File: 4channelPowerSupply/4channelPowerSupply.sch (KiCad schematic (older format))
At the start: 0 parts

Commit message: Added main components
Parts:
- added C? (x4): 4.7uF, Capacitor_SMD:C_0603_1608Metric, symbol Device:C
- added C?: 10uF, Capacitor_SMD:C_0603_1608Metric, symbol Device:C
- added C?: 2200pF, Capacitor_SMD:C_0603_1608Metric, symbol Device:C
- added C? (x2): 22pF, Capacitor_SMD:C_0603_1608Metric, symbol Device:C
- added C?: 47uF, Capacitor_SMD:C_0603_1608Metric, symbol Device:C
- added C?: 10pF, Capacitor_SMD:C_0603_1608Metric, symbol Device:C
- added C? (x3): 22uF, Capacitor_SMD:C_0603_1608Metric, symbol Device:C
- added C? (x2): 0.1uF, Capacitor_SMD:C_0603_1608Metric, symbol Device:C
- added C?: 4.7pF, Capacitor_SMD:C_0603_1608Metric, symbol Device:C
- added L?: PM1008S-1R8M-RC, Inductor_SMD:L_1008_2520Metric_Pad1.43x2.20mm_HandSolder, symbol Device:L
- added L? (x2): LPS4018-222MRC, Inductor_SMD:L_Coilcraft_XxL4020, symbol Device:L
- added L?: SDR7030-6R2M, Inductor_SMD:L_Bourns_SRP7028A_7.3x6.6mm, symbol Device:L
- added R?: 60.4, Resistor_SMD:R_0603_1608Metric, symbol Device:R
- added R?: 20K, Resistor_SMD:R_0603_1608Metric, symbol Device:R
- added R? (x2): 100K, Resistor_SMD:R_0603_1608Metric, symbol Device:R
- added R?: 249K, Resistor_SMD:R_0603_1608Metric, symbol Device:R
- added R?: 200K, Resistor_SMD:R_0603_1608Metric, symbol Device:R
- added R?: 316K, Resistor_SMD:R_0603_1608Metric, symbol Device:R
- added R?: 137K, Resistor_SMD:R_0603_1608Metric, symbol Device:R
- added R?: 453K, Resistor_SMD:R_0603_1608Metric, symbol Device:R
- added R?: 113K, Resistor_SMD:R_0603_1608Metric, symbol Device:R
- added U?: LT8602EUJ#PBF, Package_DFN_QFN:QFN-40-1EP_6x6mm_P0.5mm_EP4.6x4.6mm_ThermalVias, symbol locallib:LT8602EUJ#PBF
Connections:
- net labels added: GND
- wire segments 0 -> 136
- no-connect marks 0 -> 5

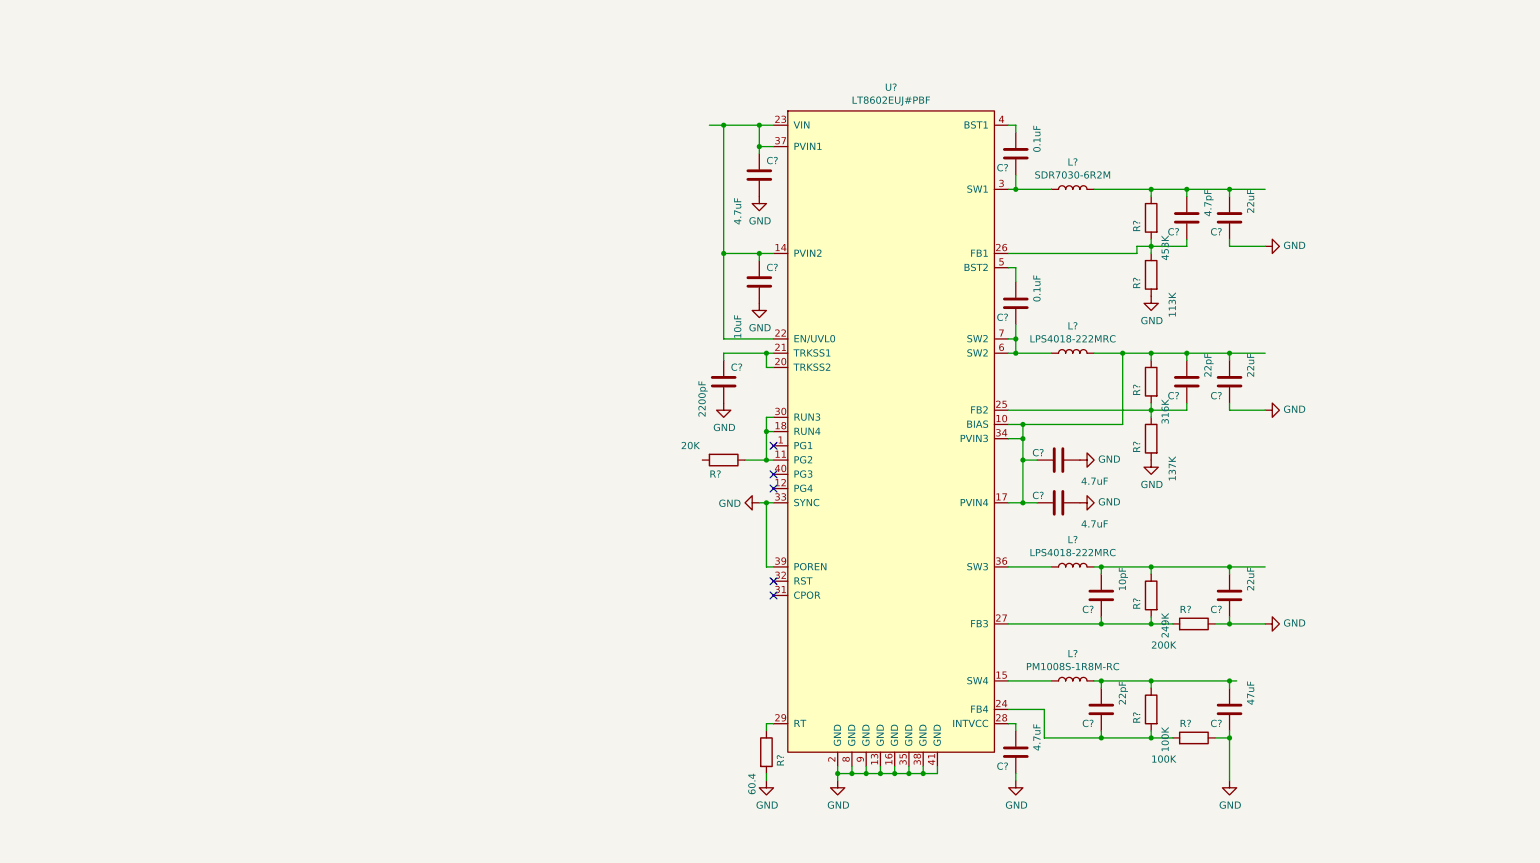
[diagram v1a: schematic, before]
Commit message: Net generated and added all components
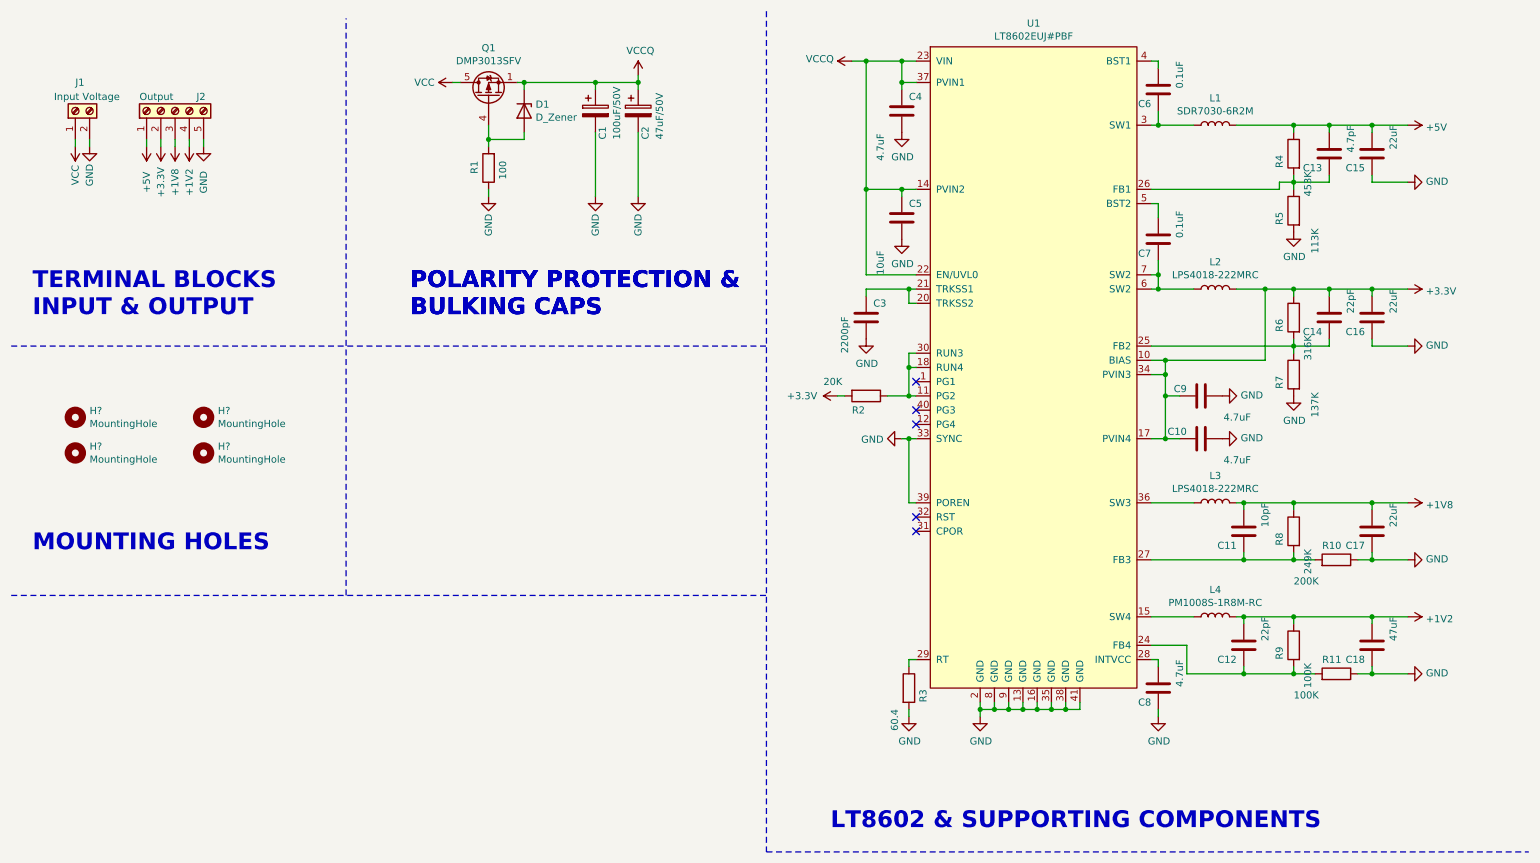
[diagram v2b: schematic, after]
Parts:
- added C1: 100uF/50V, Capacitor_SMD:C_Elec_6.3x5.4, symbol Device:CP
- added C2: 47uF/50V, Capacitor_SMD:C_Elec_6.3x5.4, symbol Device:CP
- added D1: D_Zener, symbol Device:D_Zener
- added H? (x4): MountingHole, MountingHole:MountingHole_3.2mm_M3_Pad_Via, symbol Mechanical:MountingHole
- added J1: Input Voltage, TerminalBlock_Phoenix:TerminalBlock_Phoenix_MKDS-1,5-2_1x02_P5.00mm_Horizontal, symbol Connector:Screw_Terminal_01x02
- added J2: Output, TerminalBlock_Phoenix:TerminalBlock_Phoenix_MKDS-1,5-5-5.08_1x05_P5.08mm_Horizontal, symbol Connector:Screw_Terminal_01x05
- added Q1: DMP3013SFV, Package_SON:Diodes_PowerDI3333-8, symbol Transistor_FET:DMP3013SFV
- added R1: 100, Resistor_SMD:R_0603_1608Metric, symbol Device:R
- gave numbers to parts that had none: 31
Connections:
- net labels added: +1V2, +1V8, +3.3V, +5V, VCC, VCCQ
- wire segments 136 -> 159
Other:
- note added: "LT8602 & SUPPORTING COMPONENTS"
- note added: "MOUNTING HOLES"
- note added: "POLARITY PROTECTION &\nBULKING CAPS\n"
- note added: "TERMINAL BLOCKS\nINPUT & OUTPUT"
- moved on the sheet: C10, C11, C12, C13, C14, C15, C16, C17, C18, C3, C4, C5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

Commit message: Added indication
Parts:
- added D? (x4): LED, LED_SMD:LED_0603_1608Metric, symbol Device:LED
- added R?: 900, Resistor_SMD:R_0603_1608Metric, symbol Device:R
- added R?: 600, Resistor_SMD:R_0603_1608Metric, symbol Device:R
- added R?: 1K5, Resistor_SMD:R_0603_1608Metric, symbol Device:R
- added R?: 2K5, Resistor_SMD:R_0603_1608Metric, symbol Device:R
- gave numbers to parts that had none: 4
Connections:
- net +1V2: now also R?.1
- net +1V8: now also R?.1
- net +3V3: now also R?.1
- net +5V: now also R?.1
- net GND: now also D?.1 (K), D?.1 (K), D?.1 (K), D?.1 (K)
- new net: D?.2 (A), R?.2 (x4)
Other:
- note added: "POWER INDICATION\n"
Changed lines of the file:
@@
 	1    0    0    -1
 $EndComp
-Text Notes 650  2650 0    118  ~ 24
+Text Notes 550  2750 0    118  ~ 24
 TERMINAL BLOCKS\nINPUT & OUTPUT
-Text Notes 3300 2650 0    118  ~ 24
-POLARITY PROTECTION &\nBULKING CAPS\n
-Text Notes 3300 2650 0    118  ~ 24
+Text Notes 2950 2750 0    118  ~ 24
 POLARITY PROTECTION &\nBULKING CAPS\n
 Text Notes 6250 6250 0    118  ~ 24
 LT8602 & SUPPORTING COMPONENTS
 $Comp
-L Mechanical:MountingHole H?
+L Mechanical:MountingHole H1
 U 1 1 60D5E110
 P 950 3350
-F 0 "H?" H 1050 3396 50  0000 L CNN
+F 0 "H1" H 1050 3396 50  0000 L CNN
 F 1 "MountingHole" H 1050 3305 50  0000 L CNN
 F 2 "MountingHole:MountingHole_3.2mm_M3_Pad_Via" H 950 3350 50  0001 C CNN
@@
 $EndComp
 $Comp
-L Mechanical:MountingHole H?
+L Mechanical:MountingHole H3
 U 1 1 60D5E583
 P 1850 3350
-F 0 "H?" H 1950 3396 50  0000 L CNN
+F 0 "H3" H 1950 3396 50  0000 L CNN
 F 1 "MountingHole" H 1950 3305 50  0000 L CNN
 F 2 "MountingHole:MountingHole_3.2mm_M3_Pad_Via" H 1850 3350 50  0001 C CNN
@@
 $EndComp
 $Comp
-L Mechanical:MountingHole H?
+L Mechanical:MountingHole H2
 U 1 1 60D5E8C4
 P 950 3600
-F 0 "H?" H 1050 3646 50  0000 L CNN
+F 0 "H2" H 1050 3646 50  0000 L CNN
 F 1 "MountingHole" H 1050 3555 50  0000 L CNN
 F 2 "MountingHole:MountingHole_3.2mm_M3_Pad_Via" H 950 3600 50  0001 C CNN
@@
 $EndComp
 $Comp
-L Mechanical:MountingHole H?
+L Mechanical:MountingHole H4
 U 1 1 60D5EBB4
 P 1850 3600
-F 0 "H?" H 1950 3646 50  0000 L CNN
+F 0 "H4" H 1950 3646 50  0000 L CNN
 F 1 "MountingHole" H 1950 3555 50  0000 L CNN
 F 2 "MountingHole:MountingHole_3.2mm_M3_Pad_Via" H 1850 3600 50  0001 C CNN
@@
 	1    0    0    -1
 $EndComp
-Text Notes 650  4300 0    118  ~ 24
+Text Notes 550  4500 0    118  ~ 24
 MOUNTING HOLES
 Wire Notes Line
@@
 Wire Notes Line
 	2850 4600 2850 550
+$Comp
+L power:+5V #PWR?
+U 1 1 60D89EAC
+P 4650 3300
+F 0 "#PWR?" H 4650 3150 50  0001 C CNN
+F 1 "+5V" V 4650 3550 50  0000 C CNN
+F 2 "" H 4650 3300 50  0001 C CNN
+F 3 "" H 4650 3300 50  0001 C CNN
+	1    4650 3300
+	1    0    0    -1
+$EndComp
+$Comp
+L power:+3.3V #PWR?
+U 1 1 60D89EB6
+P 4350 3300
+F 0 "#PWR?" H 4350 3150 50  0001 C CNN
+F 1 "+3.3V" V 4350 3550 50  0000 C CNN
+F 2 "" H 4350 3300 50  0001 C CNN
+F 3 "" H 4350 3300 50  0001 C CNN
+	1    4350 3300
+	1    0    0    -1
+$EndComp
+$Comp
+L power:+1V8 #PWR?
+U 1 1 60D89EC0
+P 4050 3300
+F 0 "#PWR?" H 4050 3150 50  0001 C CNN
+F 1 "+1V8" V 4050 3550 50  0000 C CNN
+F 2 "" H 4050 3300 50  0001 C CNN
+F 3 "" H 4050 3300 50  0001 C CNN
+	1    4050 3300
+	1    0    0    -1
+$EndComp
+$Comp
+L power:+1V2 #PWR?
+U 1 1 60D89ECA
+P 3750 3300
+F 0 "#PWR?" H 3750 3150 50  0001 C CNN
+F 1 "+1V2" V 3750 3550 50  0000 C CNN
+F 2 "" H 3750 3300 50  0001 C CNN
+F 3 "" H 3750 3300 50  0001 C CNN
+	1    3750 3300
+	1    0    0    -1
+$EndComp
+$Comp
+L Device:R R?
+U 1 1 60D92CCC
+P 4050 3500
+F 0 "R?" H 4120 3546 50  0000 L CNN
+F 1 "900" H 4120 3455 50  0000 L CNN
+F 2 "Resistor_SMD:R_0603_1608Metric" V 3980 3500 50  0001 C CNN
+F 3 "~" H 4050 3500 50  0001 C CNN
+F 4 "900OHM/1/4W" H 4050 3500 50  0001 C CNN "Characteristics"
+	1    4050 3500
+	1    0    0    -1
+$EndComp
+$Comp
+L Device:R R?
+U 1 1 60D9351C
+P 3750 3500
+F 0 "R?" H 3820 3546 50  0000 L CNN
+F 1 "600" H 3820 3455 50  0000 L CNN
+F 2 "Resistor_SMD:R_0603_1608Metric" V 3680 3500 50  0001 C CNN
+F 3 "~" H 3750 3500 50  0001 C CNN
+F 4 "600OHM/1/4W" H 3750 3500 50  0001 C CNN "Characteristics"
+	1    3750 3500
+	1    0    0    -1
+$EndComp
+$Comp
+L Device:R R?
+U 1 1 60D93985
+P 4350 3500
+F 0 "R?" H 4420 3546 50  0000 L CNN
+F 1 "1K5" H 4420 3455 50  0000 L CNN
+F 2 "Resistor_SMD:R_0603_1608Metric" V 4280 3500 50  0001 C CNN
+F 3 "~" H 4350 3500 50  0001 C CNN
+F 4 "1.5KOHM/1/4W" H 4350 3500 50  0001 C CNN "Characteristics"
+	1    4350 3500
+	1    0    0    -1
+$EndComp
+$Comp
+L Device:R R?
+U 1 1 60D93C3B
+P 4650 3500
+F 0 "R?" H 4720 3546 50  0000 L CNN
+F 1 "2K5" H 4720 3455 50  0000 L CNN
+F 2 "Resistor_SMD:R_0603_1608Metric" V 4580 3500 50  0001 C CNN
+F 3 "~" H 4650 3500 50  0001 C CNN
+F 4 "2.5KOHM/1/4W" H 4650 3500 50  0001 C CNN "Characteristics"
+	1    4650 3500
+	1    0    0    -1
+$EndComp
+$Comp
+L Device:LED D?
+U 1 1 60D94C55
+P 3750 3850
+F 0 "D?" V 3800 3800 50  0000 R CNN
+F 1 "LED" V 3700 3800 50  0000 R CNN
+F 2 "LED_SMD:LED_0603_1608Metric" H 3750 3850 50  0001 C CNN
+F 3 "~" H 3750 3850 50  0001 C CNN
+	1    3750 3850
+	0    -1   -1   0
+$EndComp
+$Comp
+L Device:LED D?
+U 1 1 60D952CA
+P 4050 3850
+F 0 "D?" V 4100 3800 50  0000 R CNN
+F 1 "LED" V 4000 3800 50  0000 R CNN
+F 2 "LED_SMD:LED_0603_1608Metric" H 4050 3850 50  0001 C CNN
+F 3 "~" H 4050 3850 50  0001 C CNN
+	1    4050 3850
+	0    -1   -1   0
+$EndComp
+$Comp
+L Device:LED D?
+U 1 1 60D955BC
+P 4350 3850
+F 0 "D?" V 4400 3800 50  0000 R CNN
+F 1 "LED" V 4300 3800 50  0000 R CNN
+F 2 "LED_SMD:LED_0603_1608Metric" H 4350 3850 50  0001 C CNN
+F 3 "~" H 4350 3850 50  0001 C CNN
+	1    4350 3850
+	0    -1   -1   0
+$EndComp
+$Comp
+L Device:LED D?
+U 1 1 60D9581C
+P 4650 3850
+F 0 "D?" V 4700 3800 50  0000 R CNN
+F 1 "LED" V 4600 3800 50  0000 R CNN
+F 2 "LED_SMD:LED_0603_1608Metric" H 4650 3850 50  0001 C CNN
+F 3 "~" H 4650 3850 50  0001 C CNN
+	1    4650 3850
+	0    -1   -1   0
+$EndComp
+$Comp
+L power:GND #PWR?
+U 1 1 60DA5E06
+P 3750 4050
+F 0 "#PWR?" H 3750 3800 50  0001 C CNN
+F 1 "GND" H 3755 3877 50  0000 C CNN
+F 2 "" H 3750 4050 50  0001 C CNN
+F 3 "" H 3750 4050 50  0001 C CNN
+	1    3750 4050
+	1    0    0    -1
+$EndComp
+$Comp
+L power:GND #PWR?
+U 1 1 60DA60E5
+P 4050 4050
+F 0 "#PWR?" H 4050 3800 50  0001 C CNN
+F 1 "GND" H 4055 3877 50  0000 C CNN
+F 2 "" H 4050 4050 50  0001 C CNN
+F 3 "" H 4050 4050 50  0001 C CNN
+	1    4050 4050
+	1    0    0    -1
+$EndComp
+$Comp
+L power:GND #PWR?
+U 1 1 60DA6209
+P 4350 4050
+F 0 "#PWR?" H 4350 3800 50  0001 C CNN
+F 1 "GND" H 4355 3877 50  0000 C CNN
+F 2 "" H 4350 4050 50  0001 C CNN
+F 3 "" H 4350 4050 50  0001 C CNN
+	1    4350 4050
+	1    0    0    -1
+$EndComp
+$Comp
+L power:GND #PWR?
+U 1 1 60DA642B
+P 4650 4050
+F 0 "#PWR?" H 4650 3800 50  0001 C CNN
+F 1 "GND" H 4655 3877 50  0000 C CNN
+F 2 "" H 4650 4050 50  0001 C CNN
+F 3 "" H 4650 4050 50  0001 C CNN
+	1    4650 4050
+	1    0    0    -1
+$EndComp
+Wire Wire Line
+	3750 3300 3750 3350
+Wire Wire Line
+	3750 3650 3750 3700
+Wire Wire Line
+	3750 4000 3750 4050
+Wire Wire Line
+	4050 4050 4050 4000
+Wire Wire Line
+	4050 3700 4050 3650
+Wire Wire Line
+	4050 3350 4050 3300
+Wire Wire Line
+	4350 3300 4350 3350
+Wire Wire Line
+	4350 3650 4350 3700
+Wire Wire Line
+	4350 4000 4350 4050
+Wire Wire Line
+	4650 3350 4650 3300
+Wire Wire Line
+	4650 3650 4650 3700
+Wire Wire Line
+	4650 4000 4650 4050
+Text Notes 2900 4500 0    118  ~ 24
+POWER INDICATION\n
 $EndSCHEMATC

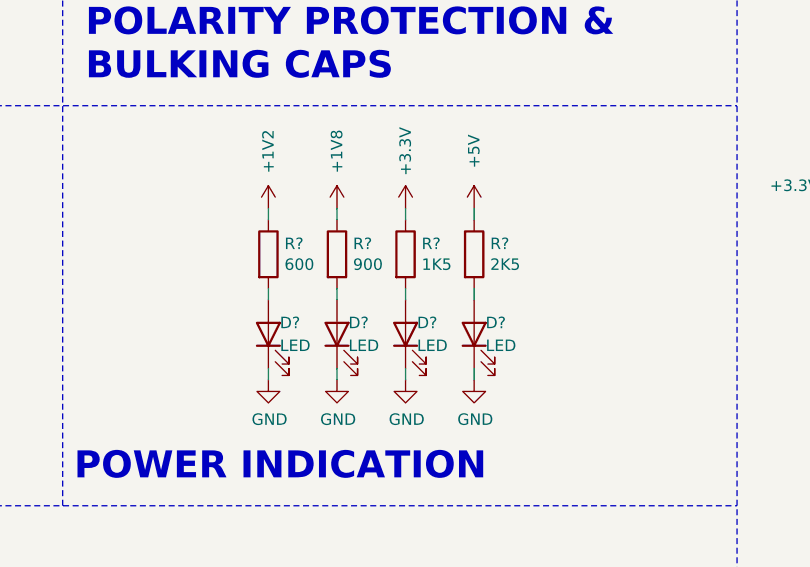
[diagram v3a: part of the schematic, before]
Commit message: Footprint for zener
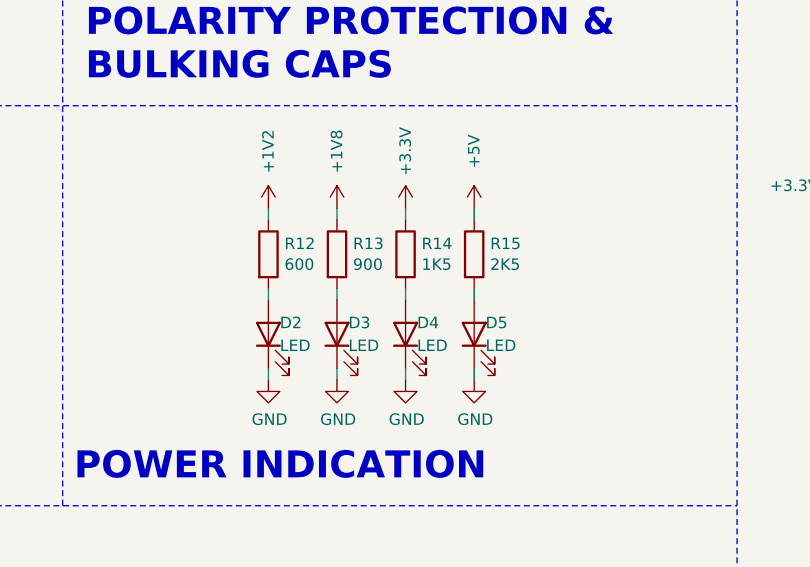
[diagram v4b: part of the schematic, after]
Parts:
- D1: footprint (none) -> Diode_SMD:D_0603_1608Metric
- gave numbers to parts that had none: 8
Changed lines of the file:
@@
 F 0 "D1" V 4054 1280 50  0000 L CNN
 F 1 "D_Zener" V 4145 1280 50  0000 L CNN
-F 2 "" H 4100 1200 50  0001 C CNN
+F 2 "Diode_SMD:D_0603_1608Metric" H 4100 1200 50  0001 C CNN
 F 3 "~" H 4100 1200 50  0001 C CNN
 	1    4100 1200
@@
 	2850 4600 2850 550
 $Comp
-L power:+5V #PWR?
+L power:+5V #PWR0134
 U 1 1 60D89EAC
 P 4650 3300
-F 0 "#PWR?" H 4650 3150 50  0001 C CNN
+F 0 "#PWR0134" H 4650 3150 50  0001 C CNN
 F 1 "+5V" V 4650 3550 50  0000 C CNN
 F 2 "" H 4650 3300 50  0001 C CNN
@@
 $EndComp
 $Comp
-L power:+3.3V #PWR?
+L power:+3.3V #PWR0135
 U 1 1 60D89EB6
 P 4350 3300
-F 0 "#PWR?" H 4350 3150 50  0001 C CNN
+F 0 "#PWR0135" H 4350 3150 50  0001 C CNN
 F 1 "+3.3V" V 4350 3550 50  0000 C CNN
 F 2 "" H 4350 3300 50  0001 C CNN
@@
 $EndComp
 $Comp
-L power:+1V8 #PWR?
+L power:+1V8 #PWR0136
 U 1 1 60D89EC0
 P 4050 3300
-F 0 "#PWR?" H 4050 3150 50  0001 C CNN
+F 0 "#PWR0136" H 4050 3150 50  0001 C CNN
 F 1 "+1V8" V 4050 3550 50  0000 C CNN
 F 2 "" H 4050 3300 50  0001 C CNN
@@
 $EndComp
 $Comp
-L power:+1V2 #PWR?
+L power:+1V2 #PWR0137
 U 1 1 60D89ECA
 P 3750 3300
-F 0 "#PWR?" H 3750 3150 50  0001 C CNN
+F 0 "#PWR0137" H 3750 3150 50  0001 C CNN
 F 1 "+1V2" V 3750 3550 50  0000 C CNN
 F 2 "" H 3750 3300 50  0001 C CNN
@@
 $EndComp
 $Comp
-L Device:R R?
+L Device:R R13
 U 1 1 60D92CCC
 P 4050 3500
-F 0 "R?" H 4120 3546 50  0000 L CNN
+F 0 "R13" H 4120 3546 50  0000 L CNN
 F 1 "900" H 4120 3455 50  0000 L CNN
 F 2 "Resistor_SMD:R_0603_1608Metric" V 3980 3500 50  0001 C CNN
@@
 $EndComp
 $Comp
-L Device:R R?
+L Device:R R12
 U 1 1 60D9351C
 P 3750 3500
-F 0 "R?" H 3820 3546 50  0000 L CNN
+F 0 "R12" H 3820 3546 50  0000 L CNN
 F 1 "600" H 3820 3455 50  0000 L CNN
 F 2 "Resistor_SMD:R_0603_1608Metric" V 3680 3500 50  0001 C CNN
@@
 $EndComp
 $Comp
-L Device:R R?
+L Device:R R14
 U 1 1 60D93985
 P 4350 3500
-F 0 "R?" H 4420 3546 50  0000 L CNN
+F 0 "R14" H 4420 3546 50  0000 L CNN
 F 1 "1K5" H 4420 3455 50  0000 L CNN
 F 2 "Resistor_SMD:R_0603_1608Metric" V 4280 3500 50  0001 C CNN
@@
 $EndComp
 $Comp
-L Device:R R?
+L Device:R R15
 U 1 1 60D93C3B
 P 4650 3500
-F 0 "R?" H 4720 3546 50  0000 L CNN
+F 0 "R15" H 4720 3546 50  0000 L CNN
 F 1 "2K5" H 4720 3455 50  0000 L CNN
 F 2 "Resistor_SMD:R_0603_1608Metric" V 4580 3500 50  0001 C CNN
@@
 $EndComp
 $Comp
-L Device:LED D?
+L Device:LED D2
 U 1 1 60D94C55
 P 3750 3850
-F 0 "D?" V 3800 3800 50  0000 R CNN
+F 0 "D2" V 3800 3800 50  0000 R CNN
 F 1 "LED" V 3700 3800 50  0000 R CNN
 F 2 "LED_SMD:LED_0603_1608Metric" H 3750 3850 50  0001 C CNN
@@
 $EndComp
 $Comp
-L Device:LED D?
+L Device:LED D3
 U 1 1 60D952CA
 P 4050 3850
-F 0 "D?" V 4100 3800 50  0000 R CNN
+F 0 "D3" V 4100 3800 50  0000 R CNN
 F 1 "LED" V 4000 3800 50  0000 R CNN
 F 2 "LED_SMD:LED_0603_1608Metric" H 4050 3850 50  0001 C CNN
@@
 $EndComp
 $Comp
-L Device:LED D?
+L Device:LED D4
 U 1 1 60D955BC
 P 4350 3850
-F 0 "D?" V 4400 3800 50  0000 R CNN
+F 0 "D4" V 4400 3800 50  0000 R CNN
 F 1 "LED" V 4300 3800 50  0000 R CNN
 F 2 "LED_SMD:LED_0603_1608Metric" H 4350 3850 50  0001 C CNN
@@
 $EndComp
 $Comp
-L Device:LED D?
+L Device:LED D5
 U 1 1 60D9581C
 P 4650 3850
-F 0 "D?" V 4700 3800 50  0000 R CNN
+F 0 "D5" V 4700 3800 50  0000 R CNN
 F 1 "LED" V 4600 3800 50  0000 R CNN
 F 2 "LED_SMD:LED_0603_1608Metric" H 4650 3850 50  0001 C CNN
@@
 $EndComp
 $Comp
-L power:GND #PWR?
+L power:GND #PWR0138
 U 1 1 60DA5E06
 P 3750 4050
-F 0 "#PWR?" H 3750 3800 50  0001 C CNN
+F 0 "#PWR0138" H 3750 3800 50  0001 C CNN
 F 1 "GND" H 3755 3877 50  0000 C CNN
 F 2 "" H 3750 4050 50  0001 C CNN
@@
 $EndComp
 $Comp
-L power:GND #PWR?
+L power:GND #PWR0139
 U 1 1 60DA60E5
 P 4050 4050
-F 0 "#PWR?" H 4050 3800 50  0001 C CNN
+F 0 "#PWR0139" H 4050 3800 50  0001 C CNN
 F 1 "GND" H 4055 3877 50  0000 C CNN
 F 2 "" H 4050 4050 50  0001 C CNN
@@
 $EndComp
 $Comp
-L power:GND #PWR?
+L power:GND #PWR0140
 U 1 1 60DA6209
 P 4350 4050
-F 0 "#PWR?" H 4350 3800 50  0001 C CNN
+F 0 "#PWR0140" H 4350 3800 50  0001 C CNN
 F 1 "GND" H 4355 3877 50  0000 C CNN
 F 2 "" H 4350 4050 50  0001 C CNN
@@
 $EndComp
 $Comp
-L power:GND #PWR?
+L power:GND #PWR0141
 U 1 1 60DA642B
 P 4650 4050
-F 0 "#PWR?" H 4650 3800 50  0001 C CNN
+F 0 "#PWR0141" H 4650 3800 50  0001 C CNN
 F 1 "GND" H 4655 3877 50  0000 C CNN
 F 2 "" H 4650 4050 50  0001 C CNN
